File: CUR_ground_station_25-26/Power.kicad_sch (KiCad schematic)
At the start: 30 parts, among them J1 Conn_01x02, J2 UJ20-C-H-G-SMT-P16-TR, Q2 NTR4003N, SW5 PTS815SJM250SMTRLFS, U2 BQ24232RGT, U3 NCP186AMX330TAG, U4 USBLC6-2SC6

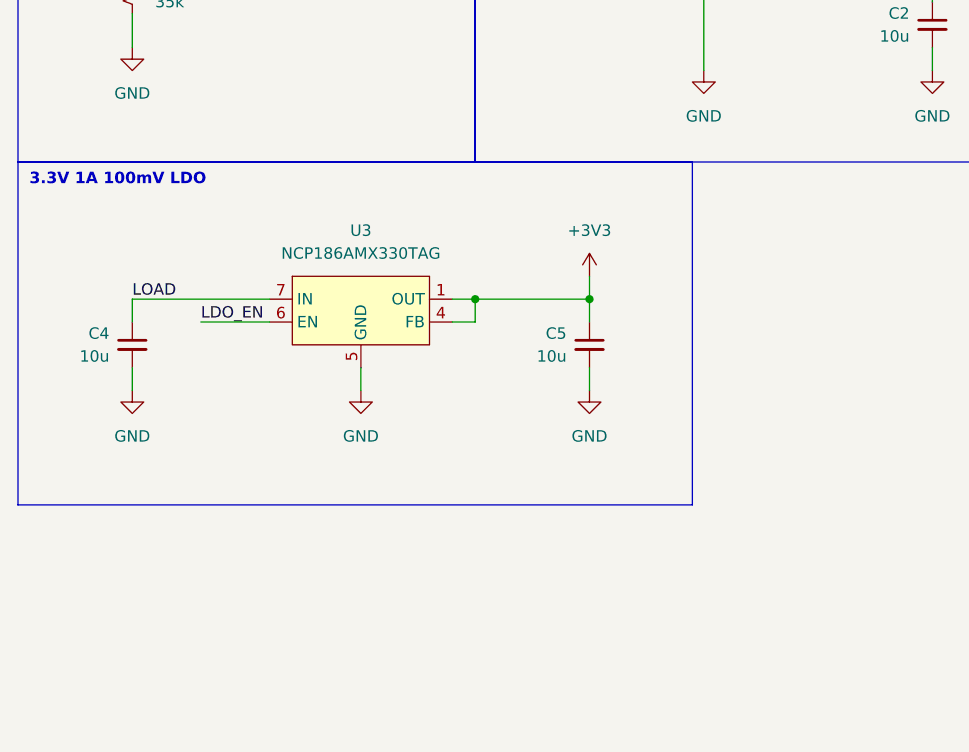
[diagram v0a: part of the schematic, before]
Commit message: added power switch
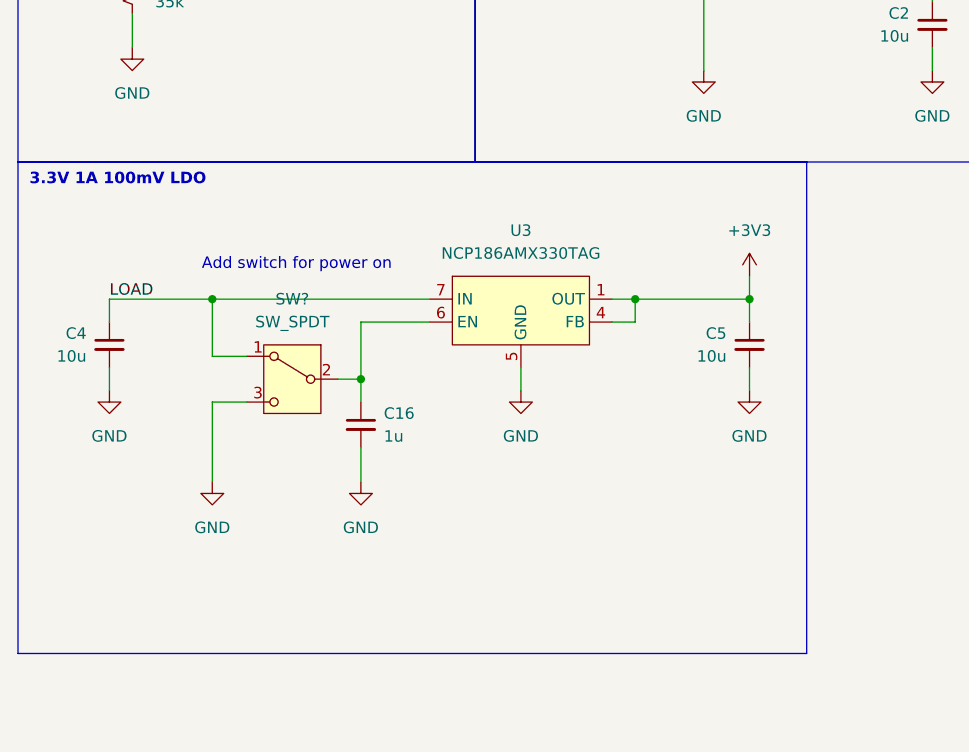
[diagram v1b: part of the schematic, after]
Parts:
- added C16: 1u, Capacitor_SMD:C_0402_1005Metric, symbol Device:C_Small
- added SW?: SW_SPDT, symbol Switch:SW_SPDT
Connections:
- net GND: now also C16.2, SW?.3 (C)
- net IN: now also SW?.1 (A)
- net LDO_EN: no longer U3.6 (EN)
- new net: C16.1, SW?.2 (B), U3.6 (EN)
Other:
- note added: "Add switch for power on"
- moved on the sheet: C4, C5, U3

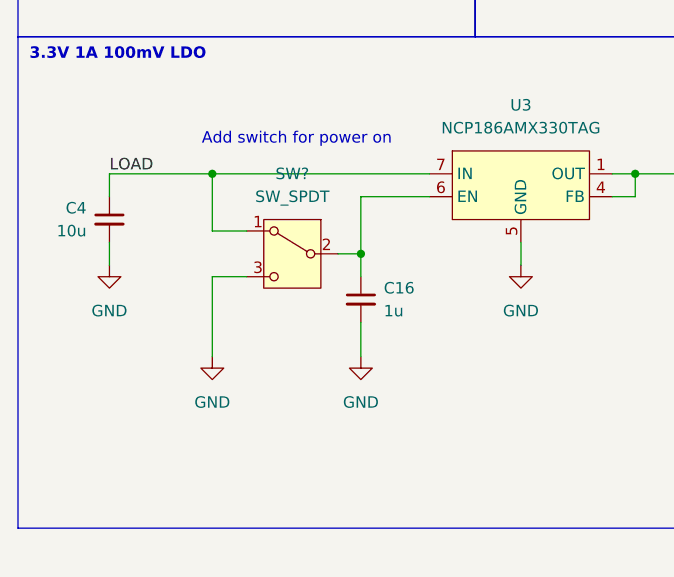
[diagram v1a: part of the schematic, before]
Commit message: ignore the fact I added a switch
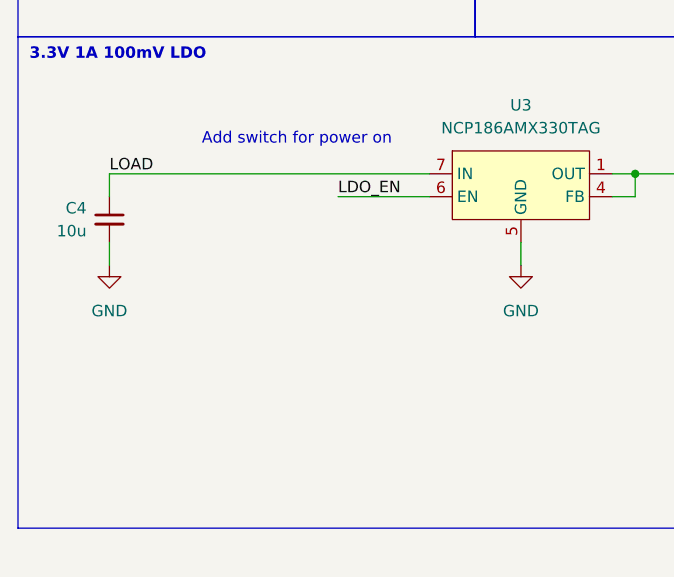
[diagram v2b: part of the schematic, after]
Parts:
- removed C16: 1u, Capacitor_SMD:C_0402_1005Metric, symbol Device:C_Small
- removed SW?: SW_SPDT, symbol Switch:SW_SPDT
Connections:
- net LDO_EN: now also U3.6 (EN)

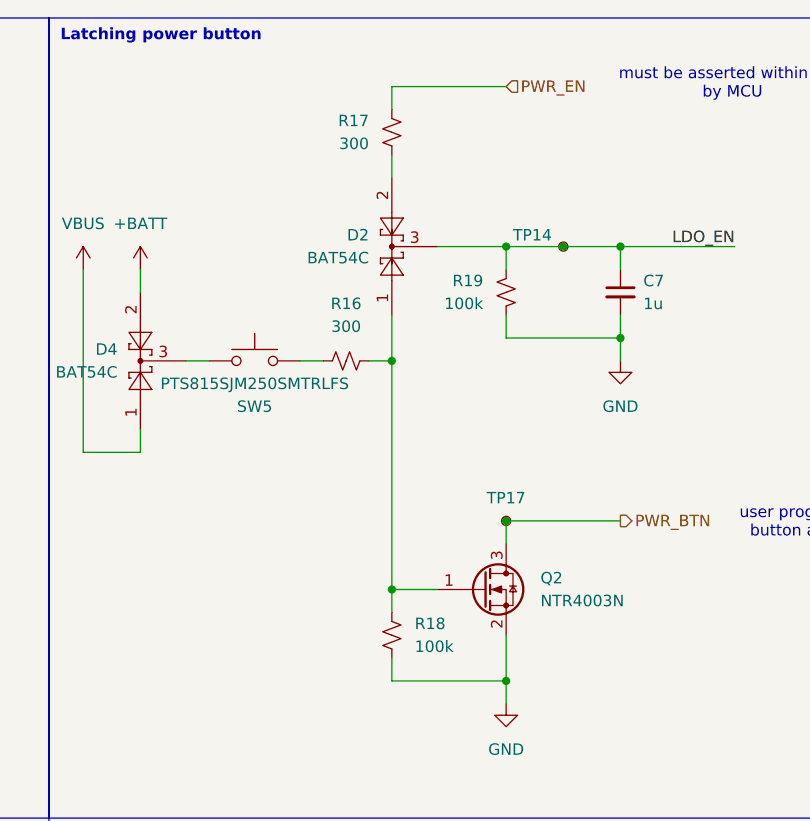
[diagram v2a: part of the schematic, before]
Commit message: BOM optimization
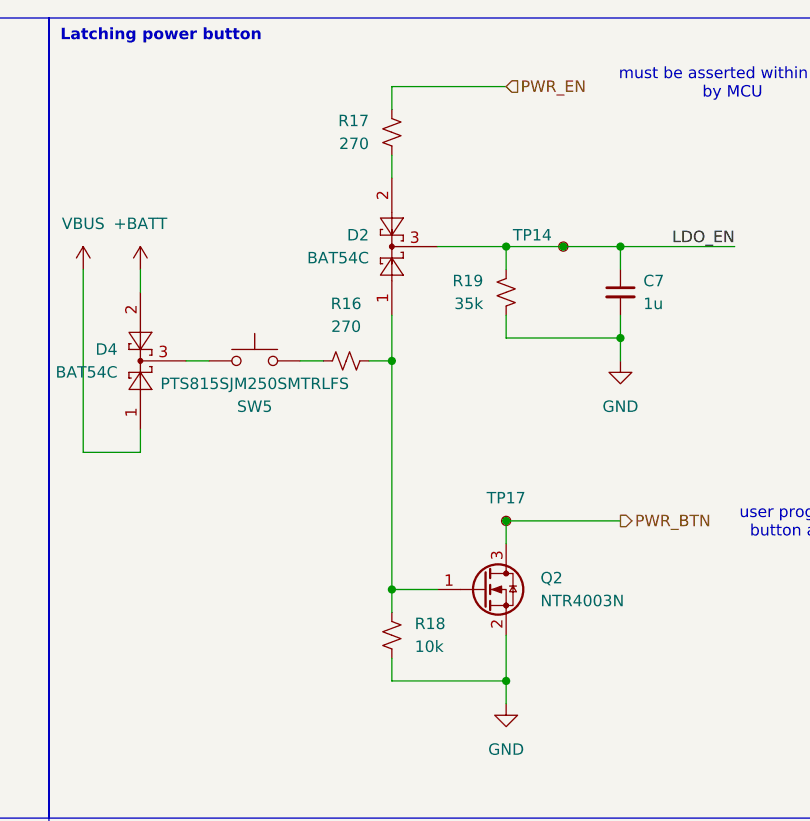
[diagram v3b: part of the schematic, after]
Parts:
- C7: footprint Capacitor_SMD:C_0402_1005Metric -> Capacitor_SMD:C_0603_1608Metric
- R16, R17: value 300 -> 270
- R18: value 100k -> 10k
- R19: value 100k -> 35k
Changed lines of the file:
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@@
 			)
 		)
-		(property "Footprint" "Capacitor_SMD:C_0402_1005Metric"
+		(property "Footprint" "Capacitor_SMD:C_0603_1608Metric"
 			(at 241.3 43.18 0)
 			(effects
@@
 			)
 		)
-		(property "Value" "100k"
+		(property "Value" "35k"
 			(at 226.06 44.4499 0)
 			(effects
@@
 			)
 		)
-		(property "Value" "300"
+		(property "Value" "270"
 			(at 213.36 26.6699 0)
 			(effects
@@
 			)
 		)
-		(property "Value" "300"
+		(property "Value" "270"
 			(at 210.82 46.99 90)
 			(effects
@@
 			)
 		)
-		(property "Value" "100k"
+		(property "Value" "10k"
 			(at 218.44 82.5499 0)
 			(effects

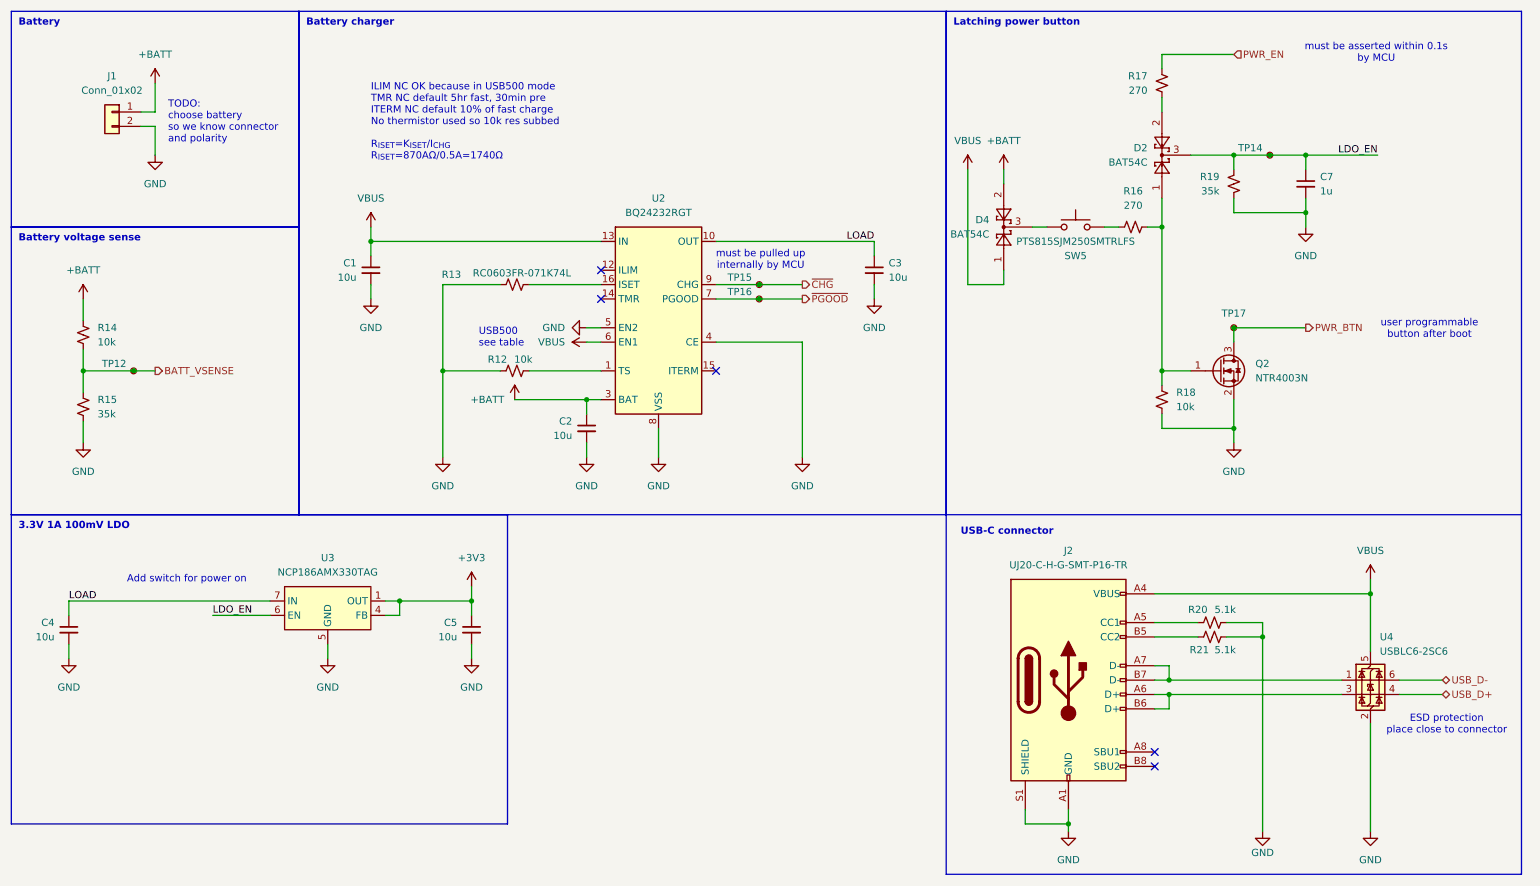
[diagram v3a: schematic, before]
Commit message: Increase RC delay on power button
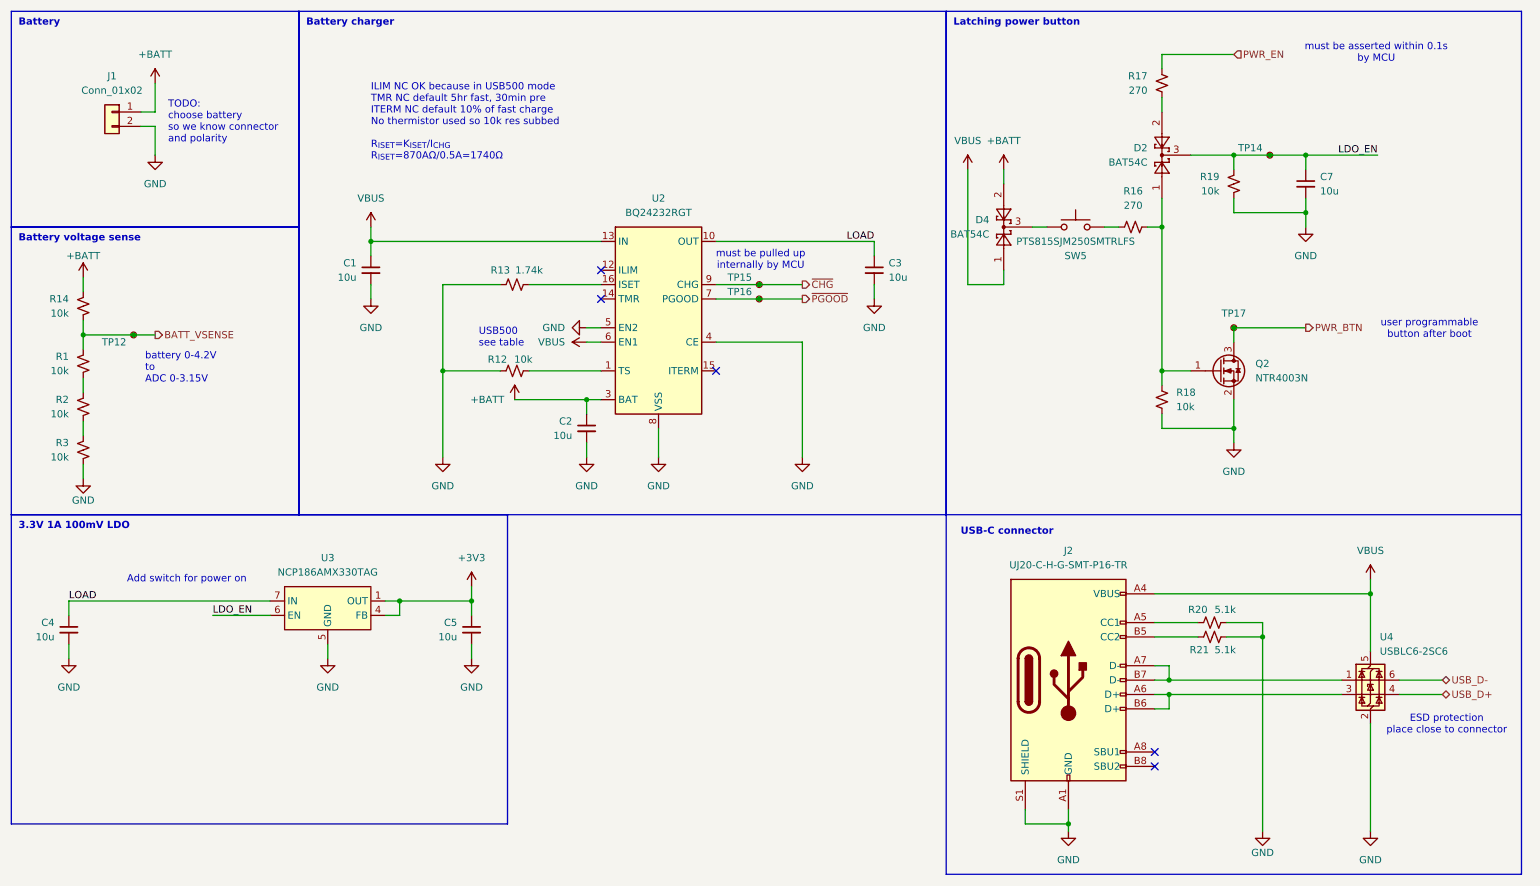
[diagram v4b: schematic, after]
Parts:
- removed R15: 35k, Resistor_SMD:R_0603_1608Metric, symbol Device:R_Small_US
- added R1, R2, R3: 10k, Resistor_SMD:R_0603_1608Metric, symbol Device:R_Small_US
- C7: value 1u -> 10u
- R13: value RC0603FR-071K74L -> 1.74k
- R19: value 35k -> 10k
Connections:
- net BATT_VSENSE: now also R1.1
- net GND: now also R3.2
- new net: R1.2, R2.1
- new net: R2.2, R3.1
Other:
- note added: "battery 0-4.2V to ADC 0-3.15V"
- moved on the sheet: R14, TP12

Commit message: Add MPNs
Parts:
- C1, C2, C3, C4, C5, C7: MPN (none) -> CL10A106MA8NRNC
- D2, D4: MPN (none) -> BAT54CLT1G
- Q2: MPN (none) -> NTR4003N
- R1, R12, R14, R18, R19, R2, R3: MPN (none) -> RC0603FR-0710KL
- R13: MPN (none) -> RC0603FR-071K74L
- R16, R17: MPN (none) -> RC0603FR-07270RL
- SW5: MPN (none) -> TS1145A16025
- U2: MPN (none) -> BQ24232RGTR
- U3: MPN (none) -> NCP186AMX330TAG
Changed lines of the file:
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@@
 			)
 		)
+		(property "MPN" "CL10A106MA8NRNC"
+			(at 93.98 121.92 0)
+			(effects
+				(font
+					(size 1.27 1.27)
+				)
+				(hide yes)
+			)
+		)
 		(pin "1"
 		)
@@
 			)
 		)
+		(property "MPN" "CL10A106MA8NRNC"
+			(at 241.3 43.18 0)
+			(effects
+				(font
+					(size 1.27 1.27)
+				)
+				(hide yes)
+			)
+		)
 		(pin "2"
 		)
@@
 			)
 		)
+		(property "MPN" "BQ24232RGTR"
+			(at 127 68.58 0)
+			(effects
+				(font
+					(size 1.27 1.27)
+				)
+				(hide yes)
+			)
+		)
 		(pin "17"
 		)
@@
 			)
 		)
+		(property "MPN" "NCP186AMX330TAG"
+			(at 68.58 114.3 0)
+			(effects
+				(font
+					(size 1.27 1.27)
+				)
+				(hide yes)
+			)
+		)
 		(pin "7"
 		)
@@
 			)
 		)
+		(property "MPN" "BAT54CLT1G"
+			(at 215.9 38.1 90)
+			(effects
+				(font
+					(size 1.27 1.27)
+				)
+				(hide yes)
+			)
+		)
 		(pin "3"
 		)
@@
 			)
 		)
+		(property "MPN" "RC0603FR-0710KL"
+			(at 101.6 76.2 90)
+			(effects
+				(font
+					(size 1.27 1.27)
+				)
+				(hide yes)
+			)
+		)
 		(pin "1"
 		)
@@
 			)
 		)
+		(property "MPN" "RC0603FR-0710KL"
+			(at 25.4 64.77 0)
+			(effects
+				(font
+					(size 1.27 1.27)
+				)
+				(hide yes)
+			)
+		)
 		(pin "2"
 		)
@@
 			)
 		)
+		(property "MPN" "RC0603FR-0710KL"
+			(at 25.4 82.55 0)
+			(effects
+				(font
+					(size 1.27 1.27)
+				)
+				(hide yes)
+			)
+		)
 		(pin "2"
 		)
@@
 			)
 		)
+		(property "MPN" "CL10A106MA8NRNC"
+			(at 165.1 58.42 0)
+			(effects
+				(font
+					(size 1.27 1.27)
+				)
+				(hide yes)
+			)
+		)
 		(pin "2"
 		)
@@
 			)
 		)
+		(property "MPN" "RC0603FR-0710KL"
+			(at 228.6 43.18 0)
+			(effects
+				(font
+					(size 1.27 1.27)
+				)
+				(hide yes)
+			)
+		)
 		(pin "2"
 		)
@@
 			)
 		)
+		(property "MPN" "CL10A106MA8NRNC"
+			(at 76.2 58.42 0)
+			(effects
+				(font
+					(size 1.27 1.27)
+				)
+				(hide yes)
+			)
+		)
 		(pin "2"
 		)
@@
 			)
 		)
+		(property "MPN" "RC0603FR-071K74L"
+			(at 101.6 60.96 90)
+			(effects
+				(font
+					(size 1.27 1.27)
+				)
+				(hide yes)
+			)
+		)
 		(pin "1"
 		)
@@
 			)
 		)
+		(property "MPN" "RC0603FR-0710KL"
+			(at 25.4 74.93 0)
+			(effects
+				(font
+					(size 1.27 1.27)
+				)
+				(hide yes)
+			)
+		)
 		(pin "2"
 		)
@@
 			)
 		)
+		(property "MPN" "BAT54CLT1G"
+			(at 187.96 50.8 90)
+			(effects
+				(font
+					(size 1.27 1.27)
+				)
+				(hide yes)
+			)
+		)
 		(pin "3"
 		)
@@
 			)
 		)
+		(property "MPN" "RC0603FR-07270RL"
+			(at 215.9 25.4 0)
+			(effects
+				(font
+					(size 1.27 1.27)
+				)
+				(hide yes)
+			)
+		)
 		(pin "2"
 		)
@@
 			)
 		)
+		(property "MPN" "TS1145A16025"
+			(at 200.66 50.8 0)
+			(effects
+				(font
+					(size 1.27 1.27)
+				)
+				(hide yes)
+			)
+		)
 		(pin "1"
 		)
@@
 			)
 		)
+		(property "MPN" "CL10A106MA8NRNC"
+			(at 22.86 121.92 0)
+			(effects
+				(font
+					(size 1.27 1.27)
+				)
+				(hide yes)
+			)
+		)
 		(pin "1"
 		)
@@
 			)
 		)
+		(property "MPN" "CL10A106MA8NRNC"
+			(at 114.3 86.36 0)
+			(effects
+				(font
+					(size 1.27 1.27)
+				)
+				(hide yes)
+			)
+		)
 		(pin "2"
 		)
@@
 			)
 		)
+		(property "MPN" "NTR4003N"
+			(at 226.06 76.2 0)
+			(effects
+				(font
+					(size 1.27 1.27)
+				)
+				(hide yes)
+			)
+		)
 		(pin "3"
 		)
@@
 			)
 		)
+		(property "MPN" "RC0603FR-0710KL"
+			(at 25.4 90.17 0)
+			(effects
+				(font
+					(size 1.27 1.27)
+				)
+				(hide yes)
+			)
+		)
 		(pin "2"
 		)
@@
 			)
 		)
+		(property "MPN" "RC0603FR-07270RL"
+			(at 210.82 50.8 90)
+			(effects
+				(font
+					(size 1.27 1.27)
+				)
+				(hide yes)
+			)
+		)
 		(pin "1"
 		)
@@
 			(at 215.9 81.28 0)
 			(effects
+				(font
+					(size 1.27 1.27)
+				)
+				(hide yes)
+			)
+		)
+		(property "MPN" "RC0603FR-0710KL"
+			(at 215.9 81.28 0)
+			(effects
